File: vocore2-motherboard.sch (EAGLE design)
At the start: 92 parts, among them IC1 AP63205, IC2 FE1.1S, IC3 LM3671MF-3.3, IC4 LM3671MF-3.3, IC5 LM3671MF-3.3, IC6 FT232R, IC7 742G17DBV, J1 RJHSE-5381, J2 TE_1775470-8, J3 AMPHENOL_1140084168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

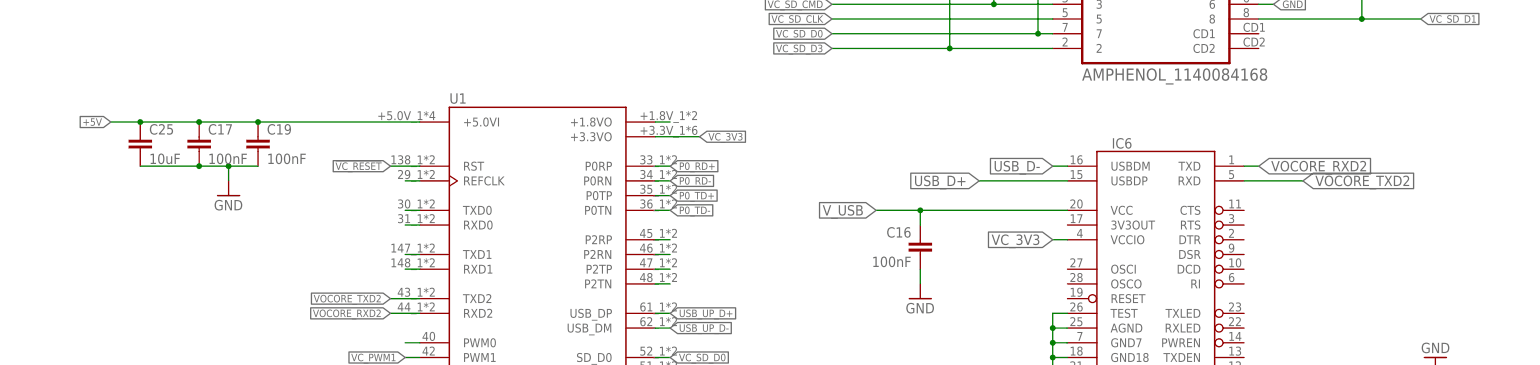
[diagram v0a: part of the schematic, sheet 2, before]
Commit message: fix(p0led): use inverting-buffer to drive lan leds
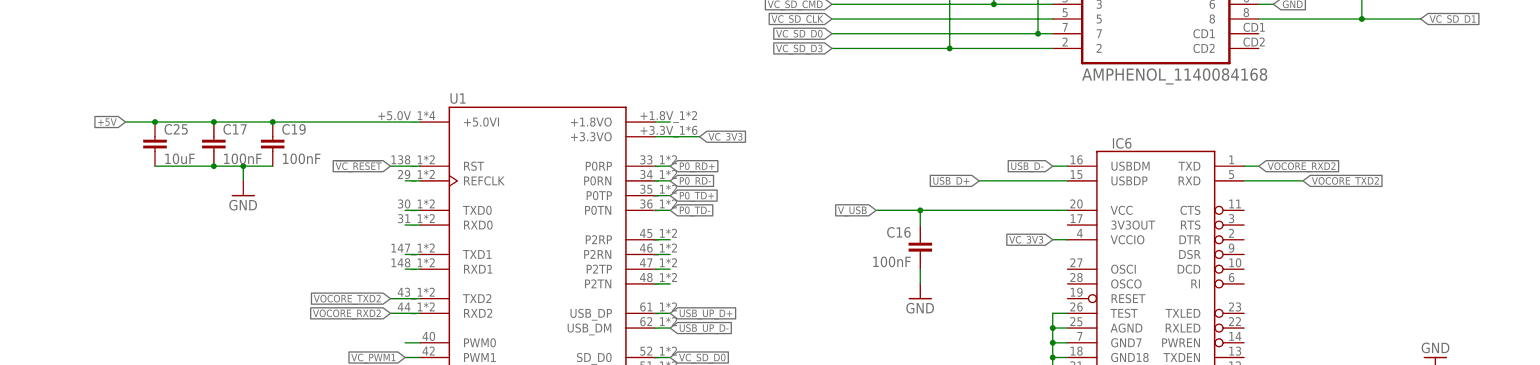
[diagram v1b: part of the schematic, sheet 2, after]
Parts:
- D2, D3: LCSC (none) -> C110478; MBM 1 -> (none); PREIS 0,393 -> (none)
- IC7: value 742G17DBV -> SN74LVC2G14DBVR; DIGIKEY 296-SN74LVC2G17DBVRCT-ND -> 296-13010-1-ND; FARNELL 1470776 -> (none)
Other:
- moved on the sheet: C17, C19, C25
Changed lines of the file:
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@@
 <part name="D3" library="diode" deviceset="DIODE-" device="SMB">
 <attribute name="FARNELL" value="1858651"/>
-<attribute name="MBM" value="1"/>
-<attribute name="PREIS" value="0,393"/>
+<attribute name="LCSC" value="C110478"/>
 </part>
 <part name="SP1" library="buzzer" library_urn="urn:adsk.eagle:library:113" deviceset="AL60P" device="" package3d_urn="urn:adsk.eagle:package:5261/1">
@@
 <part name="D2" library="diode" deviceset="DIODE-" device="SMB">
 <attribute name="FARNELL" value="1858651"/>
-<attribute name="MBM" value="1"/>
-<attribute name="PREIS" value="0,393"/>
+<attribute name="LCSC" value="C110478"/>
 </part>
 <part name="GND33" library="supply1" deviceset="GND" device=""/>
@@
 <attribute name="DIGIKEY" value="A129687CT-ND"/>
 </part>
-<part name="IC7" library="74xx-little-de" deviceset="74*2G17" device="DBV">
-<attribute name="DIGIKEY" value="296-SN74LVC2G17DBVRCT-ND"/>
-<attribute name="FARNELL" value="1470776"/>
+<part name="IC7" library="74xx-little-de" deviceset="74*2G17" device="DBV" value="SN74LVC2G14DBVR">
+<attribute name="DIGIKEY" value="296-13010-1-ND"/>
 </part>
 <part name="GND40" library="supply1" deviceset="GND" device=""/>
@@
 <instance part="D3" gate="G$1" x="38.1" y="154.94" smashed="yes">
 <attribute name="FARNELL" x="38.1" y="154.94" size="1.778" layer="96" display="off"/>
-<attribute name="MBM" x="38.1" y="154.94" size="1.778" layer="96" display="off"/>
-<attribute name="PREIS" x="38.1" y="154.94" size="1.778" layer="96" display="off"/>
 <attribute name="NAME" x="40.64" y="155.4226" size="1.778" layer="95"/>
 <attribute name="VALUE" x="40.64" y="152.6286" size="1.778" layer="96"/>
+<attribute name="LCSC" x="38.1" y="154.94" size="1.778" layer="96" display="off"/>
 </instance>
 <instance part="LED3" gate="G$1" x="27.94" y="30.48" smashed="yes">
@@
 <plain>
 <text x="45.72" y="109.22" size="1.27" layer="98">tty console</text>
-<text x="44.704" y="93.726" size="1.27" layer="98">CS0 = NOR Flash !CS</text>
+<text x="31.75" y="85.344" size="1.27" layer="98">CS0 = NOR Flash !CS</text>
 <text x="93.98" y="38.1" size="2.54" layer="97" align="bottom-center">USB Schutzbeschaltung</text>
 </plain>
@@
 <attribute name="LCSC" x="15.24" y="33.02" size="2.54" layer="96" rot="R270" display="off"/>
 </instance>
-<instance part="C17" gate="G$1" x="27.94" y="134.62" smashed="yes">
-<attribute name="NAME" x="29.464" y="135.001" size="1.778" layer="95"/>
-<attribute name="VALUE" x="29.464" y="129.921" size="1.778" layer="96"/>
-</instance>
-<instance part="C19" gate="G$1" x="38.1" y="134.62" smashed="yes">
-<attribute name="NAME" x="39.624" y="135.001" size="1.778" layer="95"/>
-<attribute name="VALUE" x="39.624" y="129.921" size="1.778" layer="96"/>
-</instance>
-<instance part="GND24" gate="1" x="33.02" y="124.46" smashed="yes">
-<attribute name="VALUE" x="30.48" y="121.92" size="1.778" layer="96"/>
+<instance part="C17" gate="G$1" x="30.48" y="134.62" smashed="yes">
+<attribute name="NAME" x="32.004" y="135.001" size="1.778" layer="95"/>
+<attribute name="VALUE" x="32.004" y="129.921" size="1.778" layer="96"/>
+</instance>
+<instance part="C19" gate="G$1" x="40.64" y="134.62" smashed="yes">
+<attribute name="NAME" x="42.164" y="135.001" size="1.778" layer="95"/>
+<attribute name="VALUE" x="42.164" y="129.921" size="1.778" layer="96"/>
+</instance>
+<instance part="GND24" gate="1" x="35.56" y="124.46" smashed="yes">
+<attribute name="VALUE" x="33.02" y="121.92" size="1.778" layer="96"/>
 </instance>
 <instance part="GND25" gate="1" x="109.22" y="45.72" smashed="yes">
@@
 <attribute name="VALUE" x="134.62" y="53.34" size="1.778" layer="96"/>
 </instance>
-<instance part="C25" gate="G$1" x="17.78" y="134.62" smashed="yes">
-<attribute name="NAME" x="19.304" y="135.001" size="1.778" layer="95"/>
-<attribute name="VALUE" x="19.304" y="129.921" size="1.778" layer="96"/>
+<instance part="C25" gate="G$1" x="20.32" y="134.62" smashed="yes">
+<attribute name="NAME" x="21.844" y="135.001" size="1.778" layer="95"/>
+<attribute name="VALUE" x="21.844" y="129.921" size="1.778" layer="96"/>
 </instance>
 <instance part="J3" gate="G$1" x="193.04" y="154.94" smashed="yes">
@@
 <segment>
 <pinref part="U1" gate="G$1" pin="+5.0VI"/>
-<wire x1="66.04" y1="137.16" x2="38.1" y2="137.16" width="0.1524" layer="91"/>
-<wire x1="38.1" y1="137.16" x2="27.94" y2="137.16" width="0.1524" layer="91"/>
-<wire x1="27.94" y1="137.16" x2="17.78" y2="137.16" width="0.1524" layer="91"/>
+<wire x1="66.04" y1="137.16" x2="40.64" y2="137.16" width="0.1524" layer="91"/>
+<wire x1="40.64" y1="137.16" x2="30.48" y2="137.16" width="0.1524" layer="91"/>
+<wire x1="30.48" y1="137.16" x2="20.32" y2="137.16" width="0.1524" layer="91"/>
 <pinref part="C17" gate="G$1" pin="1"/>
-<junction x="27.94" y="137.16"/>
+<junction x="30.48" y="137.16"/>
 <pinref part="C19" gate="G$1" pin="1"/>
-<junction x="38.1" y="137.16"/>
-<label x="12.7" y="137.16" size="1.27" layer="95" rot="R180" xref="yes"/>
+<junction x="40.64" y="137.16"/>
+<label x="15.24" y="137.16" size="1.27" layer="95" rot="R180" xref="yes"/>
 <pinref part="C25" gate="G$1" pin="1"/>
-<wire x1="17.78" y1="137.16" x2="12.7" y2="137.16" width="0.1524" layer="91"/>
-<junction x="17.78" y="137.16"/>
+<wire x1="20.32" y1="137.16" x2="15.24" y2="137.16" width="0.1524" layer="91"/>
+<junction x="20.32" y="137.16"/>
 </segment>
 <segment>
@@
 <pinref part="C17" gate="G$1" pin="2"/>
 <pinref part="C19" gate="G$1" pin="2"/>
-<wire x1="27.94" y1="129.54" x2="33.02" y2="129.54" width="0.1524" layer="91"/>
+<wire x1="30.48" y1="129.54" x2="35.56" y2="129.54" width="0.1524" layer="91"/>
 <pinref part="GND24" gate="1" pin="GND"/>
-<wire x1="33.02" y1="129.54" x2="38.1" y2="129.54" width="0.1524" layer="91"/>
-<wire x1="33.02" y1="127" x2="33.02" y2="129.54" width="0.1524" layer="91"/>
-<junction x="33.02" y="129.54"/>
+<wire x1="35.56" y1="129.54" x2="40.64" y2="129.54" width="0.1524" layer="91"/>
+<wire x1="35.56" y1="127" x2="35.56" y2="129.54" width="0.1524" layer="91"/>
+<junction x="35.56" y="129.54"/>
 <pinref part="C25" gate="G$1" pin="2"/>
-<wire x1="27.94" y1="129.54" x2="17.78" y2="129.54" width="0.1524" layer="91"/>
-<junction x="27.94" y="129.54"/>
+<wire x1="30.48" y1="129.54" x2="20.32" y2="129.54" width="0.1524" layer="91"/>
+<junction x="30.48" y="129.54"/>
 </segment>
 <segment>
@@
 <pinref part="IC6" gate="G$1" pin="RXD"/>
 <wire x1="208.28" y1="127" x2="218.44" y2="127" width="0.1524" layer="91"/>
-<label x="218.44" y="127" size="1.778" layer="95" xref="yes"/>
+<label x="218.44" y="127" size="1.27" layer="95" xref="yes"/>
 </segment>
 <segment>
@@
 <pinref part="IC6" gate="G$1" pin="TXD"/>
 <wire x1="208.28" y1="129.54" x2="210.82" y2="129.54" width="0.1524" layer="91"/>
-<label x="210.82" y="129.54" size="1.778" layer="95" xref="yes"/>
+<label x="210.82" y="129.54" size="1.27" layer="95" xref="yes"/>
 </segment>
 <segment>
@@
 <pinref part="IC6" gate="G$1" pin="VCCIO"/>
 <wire x1="177.8" y1="116.84" x2="175.26" y2="116.84" width="0.1524" layer="91"/>
-<label x="175.26" y="116.84" size="1.778" layer="95" rot="R180" xref="yes"/>
+<label x="175.26" y="116.84" size="1.27" layer="95" rot="R180" xref="yes"/>
 </segment>
 <segment>
@@
 <pinref part="IC6" gate="G$1" pin="USBDP"/>
 <wire x1="177.8" y1="127" x2="162.56" y2="127" width="0.1524" layer="91"/>
-<label x="162.56" y="127" size="1.778" layer="95" rot="R180" xref="yes"/>
+<label x="162.56" y="127" size="1.27" layer="95" rot="R180" xref="yes"/>
 </segment>
 <segment>
@@
 <pinref part="IC6" gate="G$1" pin="USBDM"/>
 <wire x1="177.8" y1="129.54" x2="175.26" y2="129.54" width="0.1524" layer="91"/>
-<label x="175.26" y="129.54" size="1.778" layer="95" rot="R180" xref="yes"/>
+<label x="175.26" y="129.54" size="1.27" layer="95" rot="R180" xref="yes"/>
 </segment>
 <segment>
@@
 <pinref part="IC6" gate="G$1" pin="VCC"/>
 <wire x1="177.8" y1="121.92" x2="152.4" y2="121.92" width="0.1524" layer="91"/>
-<label x="144.78" y="121.92" size="1.778" layer="95" rot="R180" xref="yes"/>
+<label x="144.78" y="121.92" size="1.27" layer="95" rot="R180" xref="yes"/>
 <pinref part="C16" gate="G$1" pin="1"/>
 <wire x1="152.4" y1="121.92" x2="144.78" y2="121.92" width="0.1524" layer="91"/>
@@
 <instance part="D2" gate="G$1" x="119.38" y="93.98" smashed="yes" rot="R180">
 <attribute name="FARNELL" x="119.38" y="93.98" size="1.778" layer="96" rot="R180" display="off"/>
-<attribute name="MBM" x="119.38" y="93.98" size="1.778" layer="96" rot="R180" display="off"/>
-<attribute name="PREIS" x="119.38" y="93.98" size="1.778" layer="96" rot="R180" display="off"/>
 <attribute name="NAME" x="116.84" y="93.4974" size="1.778" layer="95" rot="R180"/>
 <attribute name="VALUE" x="116.84" y="96.2914" size="1.778" layer="96" rot="R180"/>
+<attribute name="LCSC" x="119.38" y="93.98" size="1.778" layer="96" rot="R180" display="off"/>
 </instance>
 <instance part="GND33" gate="1" x="175.26" y="81.28" smashed="yes">
@@
 <attribute name="NAME" x="219.71" y="109.855" size="1.778" layer="95" font="vector" rot="MR0"/>
 <attribute name="VALUE" x="219.71" y="101.6" size="1.778" layer="96" font="vector" rot="MR0"/>
+<attribute name="DIGIKEY" x="220.98" y="106.68" size="1.778" layer="96" rot="MR0" display="off"/>
 </instance>
 <instance part="IC7" gate="B" x="220.98" y="88.9" smashed="yes" rot="R180">
 <attribute name="NAME" x="219.71" y="85.725" size="1.778" layer="95" font="vector" rot="R180"/>
 <attribute name="VALUE" x="219.71" y="93.98" size="1.778" layer="96" font="vector" rot="R180"/>
-<attribute name="DIGIKEY" x="220.98" y="88.9" size="1.778" layer="96" rot="R180" display="off"/>
 </instance>
 <instance part="IC7" gate="C" x="233.68" y="50.8" smashed="yes">
@@
 <description>Mini-PCIe &amp; USB-Hub</description>
 <plain>
-<text x="137.16" y="37.084" size="1.27" layer="98" rot="MR0">OVCJ=1: No Overcurrent detected
+<text x="116.84" y="32.004" size="1.27" layer="98" rot="MR0">OVCJ=1: No Overcurrent detected
 BUSJ=1: Host is powered up
 VBUSM=1: Self powered

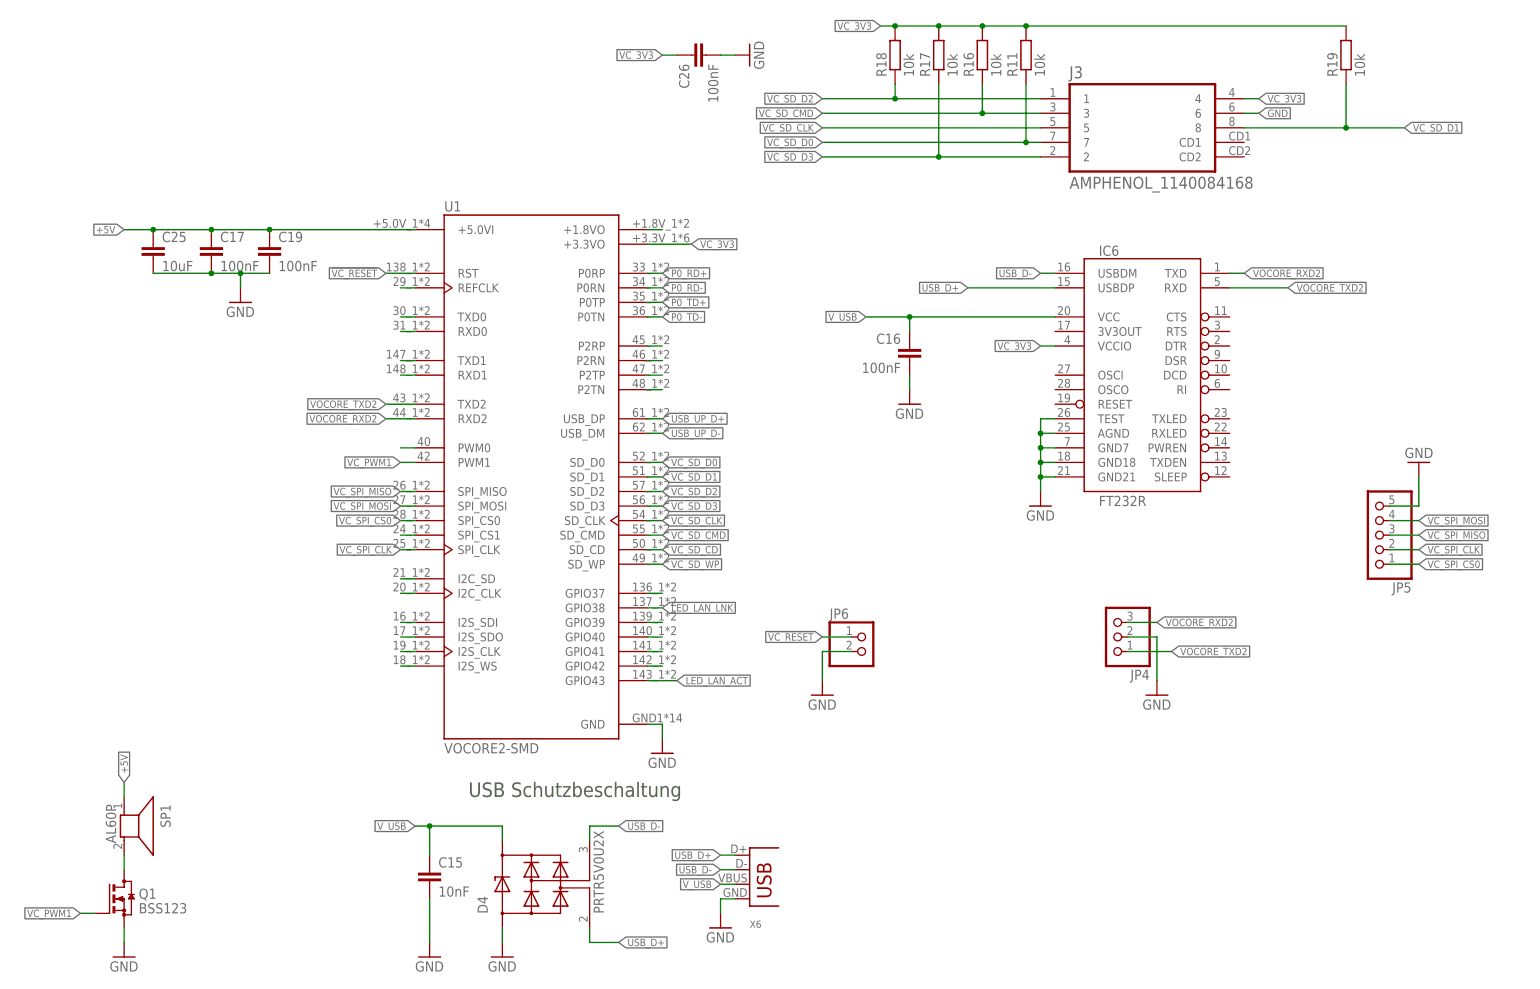
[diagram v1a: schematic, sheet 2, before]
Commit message: feat(sch): cleanup page 3 vocore & uart bridge
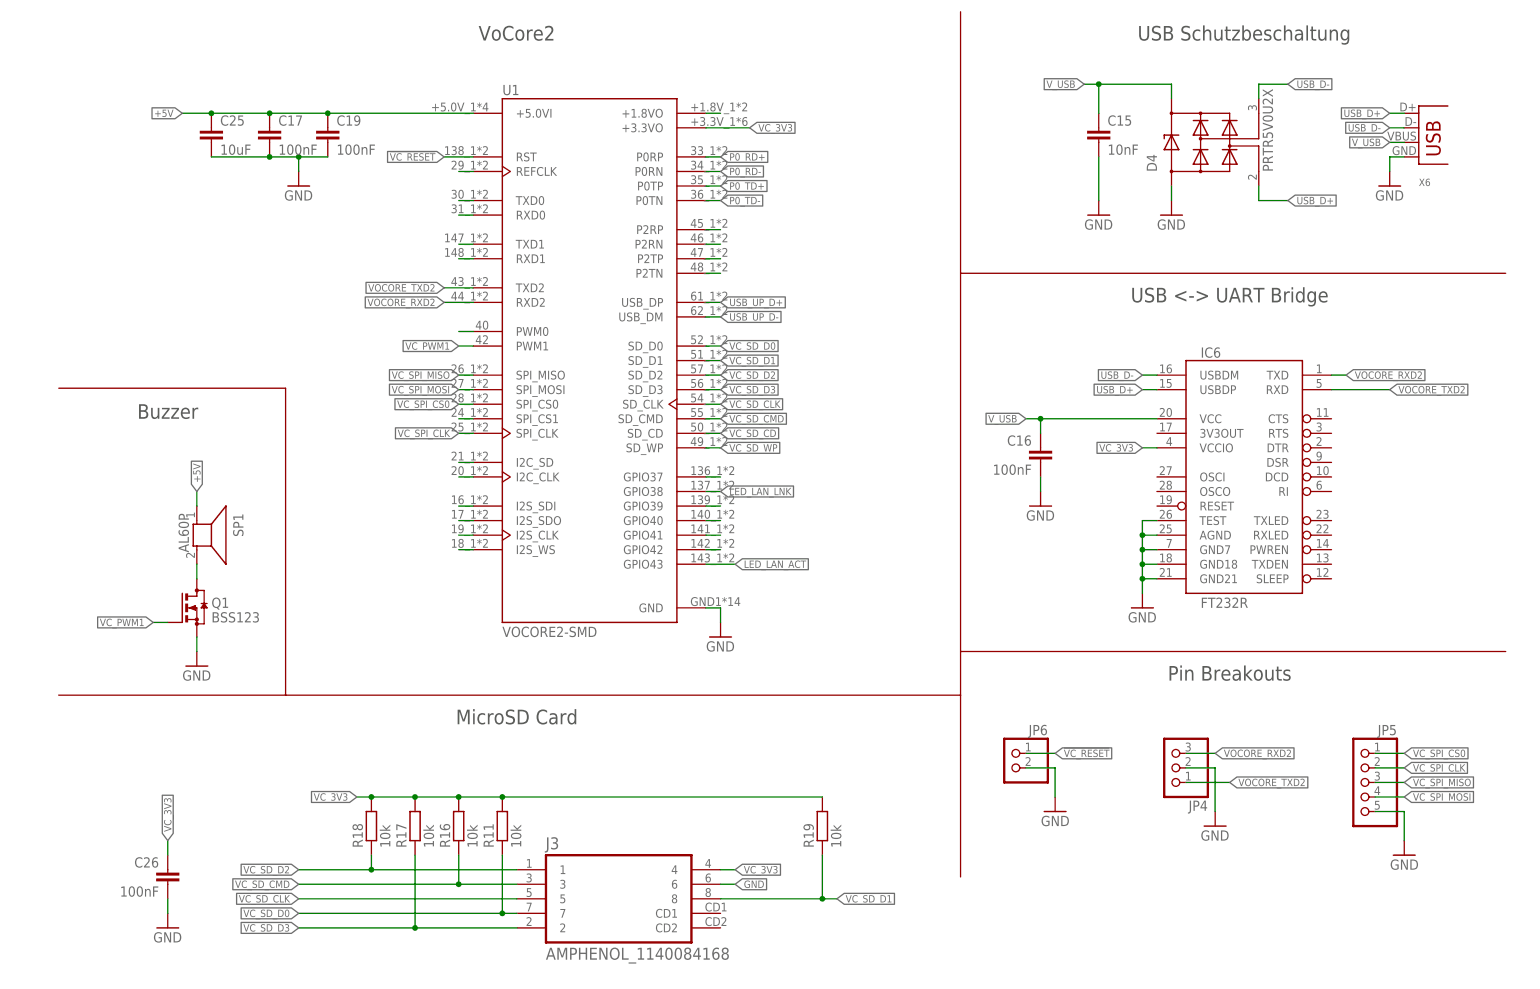
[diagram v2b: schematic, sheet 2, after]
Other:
- note added: "Buzzer"
- note added: "MicroSD Card"
- note added: "Pin Breakouts"
- note added: "USB <-> UART Bridge"
- note added: "VoCore2"
- moved on the sheet: C15, C16, C17, C19, C25, C26, D4, IC6, J3, JP4, JP5, JP6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
